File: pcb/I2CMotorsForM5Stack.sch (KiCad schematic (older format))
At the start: 14 parts, among them J1 free_holes, J2 Conn_01x04, J3 Conn_01x06, U1 TB6612FNG, U2 ATmega328P-AU

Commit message: Create pcb folder
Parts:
- U2: value ATmega328P-AU -> ATmega328P-MU; footprint Package_QFP:TQFP-32_7x7mm_P0.8mm -> Package_DFN_QFN:QFN-32-1EP_5x5mm_P0.5mm_EP3.1x3.1mm; symbol MCU_Microchip_ATmega:ATmega328P-AU -> MCU_Microchip_ATmega:ATmega328P-MU
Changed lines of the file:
@@
 $EndComp
 $Comp
-L MCU_Microchip_ATmega:ATmega328P-AU U2
+L MCU_Microchip_ATmega:ATmega328P-MU U2
 U 1 1 5E3FF990
 P 6750 3100
 F 0 "U2" H 6750 1511 50  0000 C CNN
-F 1 "ATmega328P-AU" H 6750 1420 50  0000 C CNN
-F 2 "Package_QFP:TQFP-32_7x7mm_P0.8mm" H 6750 3100 50  0001 C CIN
+F 1 "ATmega328P-MU" H 6750 1420 50  0000 C CNN
+F 2 "Package_DFN_QFN:QFN-32-1EP_5x5mm_P0.5mm_EP3.1x3.1mm" H 6750 3100 50  0001 C CIN
 F 3 "http://ww1.microchip.com/downloads/en/DeviceDoc/ATmega328_P%20AVR%20MCU%20with%20picoPower%20Technology%20Data%20Sheet%2040001984A.pdf" H 6750 3100 50  0001 C CNN
 	1    6750 3100

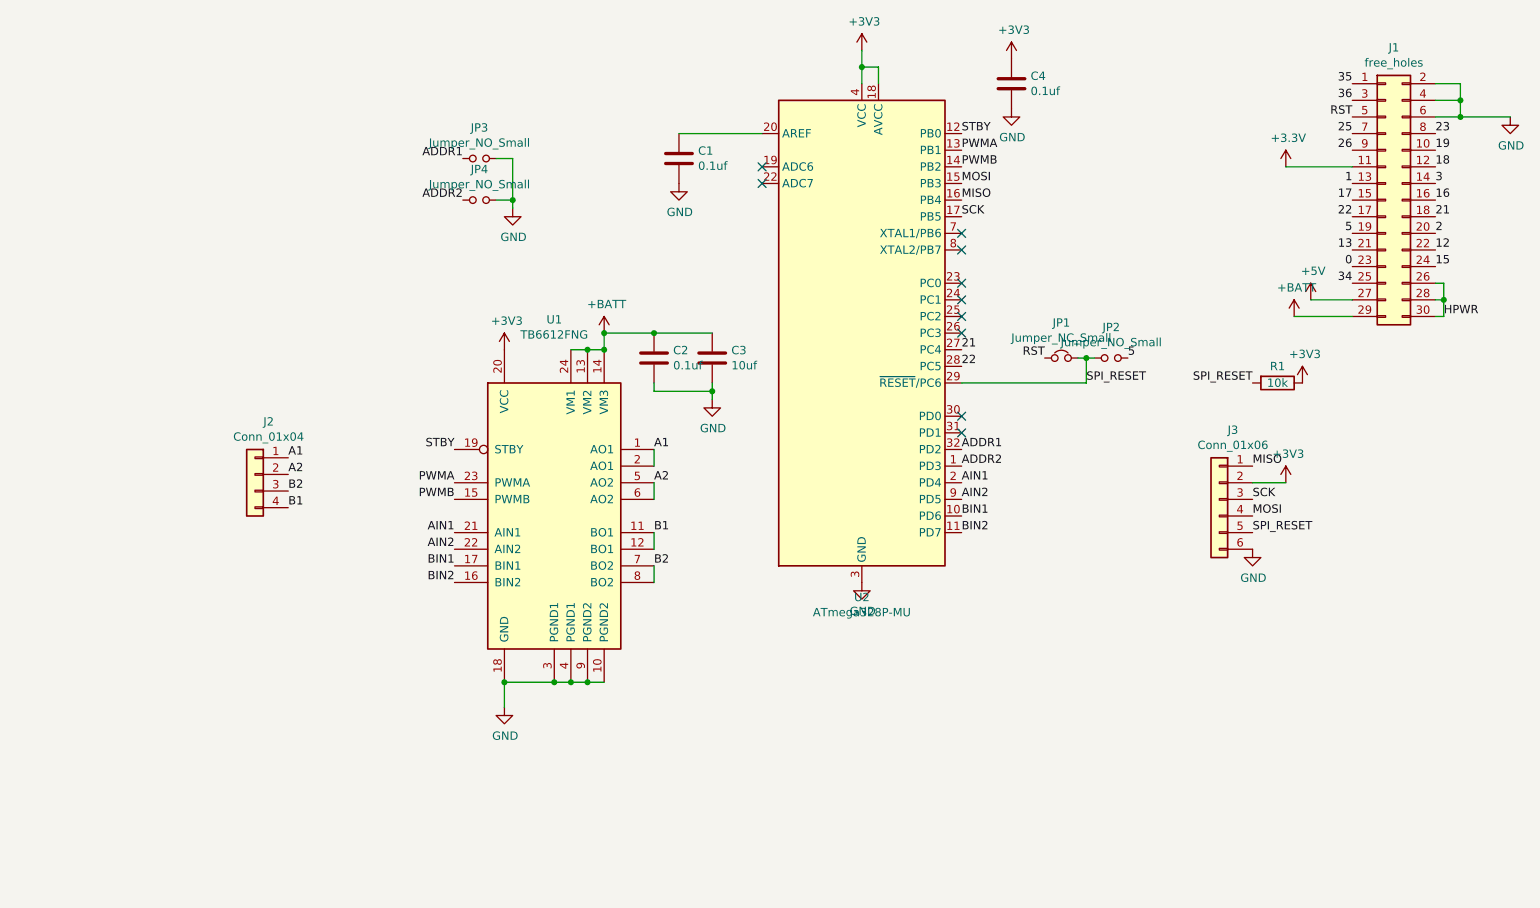
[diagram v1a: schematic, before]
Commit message: Put terminal mount out side of m5stack zone
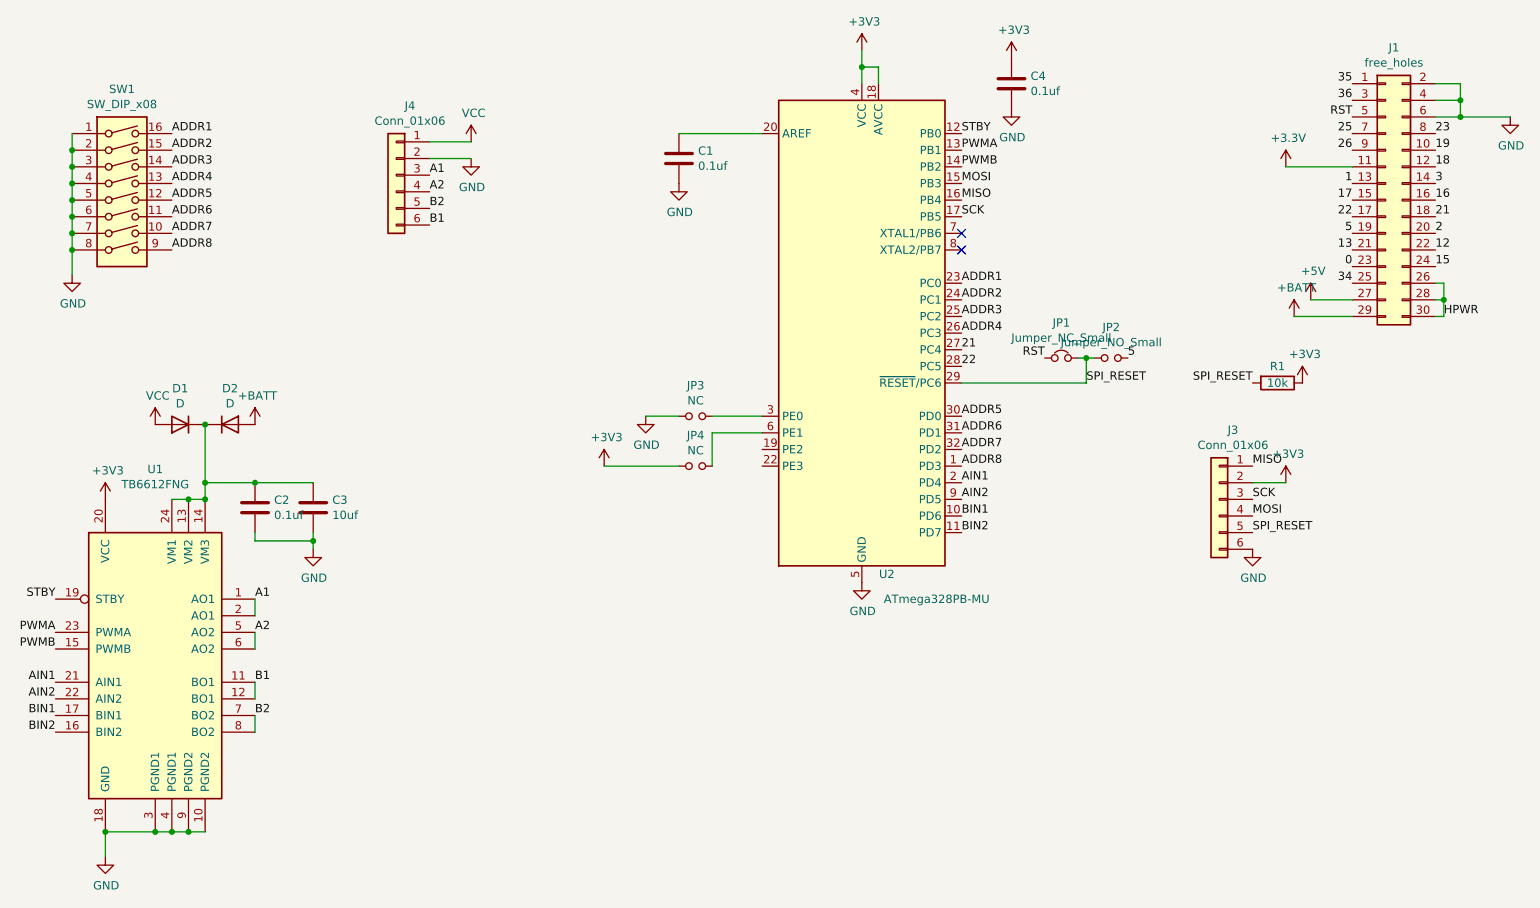
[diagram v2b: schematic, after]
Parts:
- removed J2: Conn_01x04, TerminalBlock:TerminalBlock_bornier-4_P5.08mm, symbol Connector_Generic:Conn_01x04
- removed U2: ATmega328P-MU, Package_DFN_QFN:QFN-32-1EP_5x5mm_P0.5mm_EP3.1x3.1mm, symbol MCU_Microchip_ATmega:ATmega328P-MU
- added D1, D2: D, Diode_SMD:D_SOD-123F, symbol Device:D
- added J4: Conn_01x06, TerminalBlock:TerminalBlock_bornier-6_P5.08mm, symbol Connector_Generic:Conn_01x06
- added SW1: SW_DIP_x08, Button_Switch_THT:SW_DIP_SPSTx08_Piano_CTS_Series194-8MSTN_W7.62mm_P2.54mm, symbol Switch:SW_DIP_x08
- added U2: ATmega328PB-MU, Package_DFN_QFN:QFN-32-1EP_5x5mm_P0.5mm_EP3.1x3.1mm, symbol MCU_Microchip_ATmega:ATmega328PB-MU
- J3: footprint Connector_PinHeader_2.54mm:PinHeader_2x03_P2.54mm_Vertical -> footprints:2x03_P2.54mm_Pads
- JP3, JP4: value Jumper_NO_Small -> NC
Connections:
- net +3V3: now also JP4.1, U2.18 (AVCC), U2.4 (VCC)
- net +BATT: now also D2.2 (A); no longer C2.1, C3.1, U1.13 (VM2), U1.14 (VM3), U1.24 (VM1)
- net 21: now also U2.27 (PC4)
- net 22: now also U2.28 (PC5)
- net A1: now also J4.3 (Pin_3)
- net A2: now also J4.4 (Pin_4)
- net ADDR1: now also SW1.16, U2.23 (PC0); no longer JP3.1
- net ADDR2: now also SW1.15, U2.24 (PC1); no longer JP4.1
- net AIN1: now also U2.2 (PD4)
- net AIN2: now also U2.9 (PD5)
- net B1: now also J4.6 (Pin_6)
- net B2: now also J4.5 (Pin_5)
- net BIN1: now also U2.10 (PD6)
- net BIN2: now also U2.11 (PD7)
- net GND: now also JP3.1, J4.2 (Pin_2), SW1.1, SW1.2, SW1.3, SW1.4, SW1.5, SW1.6, SW1.7, SW1.8, U2.21 (GND), U2.33 (GND), U2.5 (GND); no longer JP3.2, JP4.2
- net MISO: now also U2.16 (PB4)
- net MOSI: now also U2.15 (PB3)
- net PWMA: now also U2.13 (PB1)
- net PWMB: now also U2.14 (PB2)
- net SCK: now also U2.17 (PB5)
- net SPI_RESET: now also U2.29 (~RESET~/PC6)
- net STBY: now also U2.12 (PB0)
- net at C1.1: now also U2.20 (AREF)
- new net: C2.1, C3.1, D1.1 (K), D2.1 (K), U1.13 (VM2), U1.14 (VM3), U1.24 (VM1)
- new net: JP3.2, U2.3 (PE0)
- new net: JP4.2, U2.6 (PE1)
- new net ADDR3: SW1.14, U2.25 (PC2)
- new net ADDR4: SW1.13, U2.26 (PC3)
- new net ADDR5: SW1.12, U2.30 (PD0)
- new net ADDR6: SW1.11, U2.31 (PD1)
- new net ADDR7: SW1.10, U2.32 (PD2)
- new net ADDR8: SW1.9, U2.1 (PD3)
- new net VCC: D1.2 (A), J4.1 (Pin_1)
- no-connect marks 10 -> 2
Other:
- moved on the sheet: C2, C3, U1

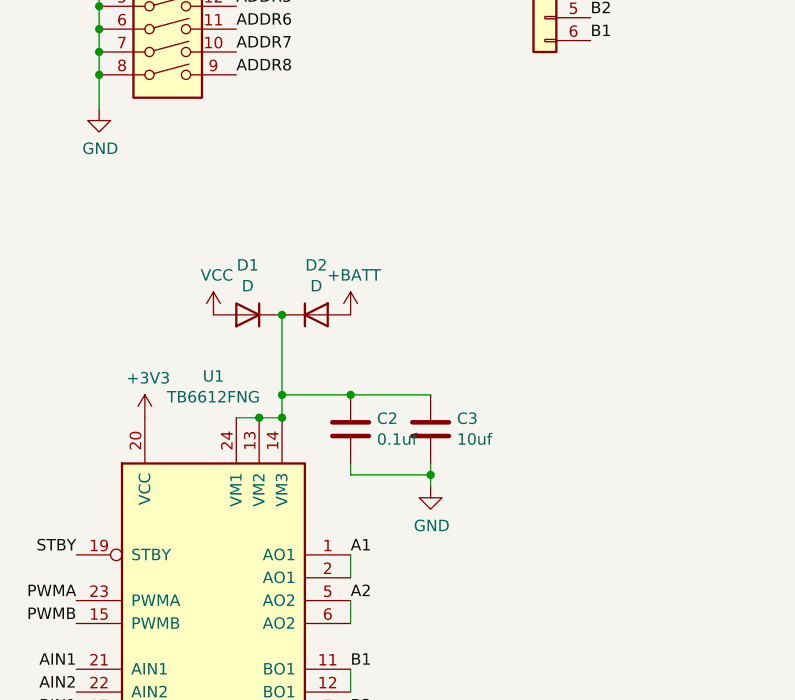
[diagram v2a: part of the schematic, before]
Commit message: Add diode to connect VM and GND
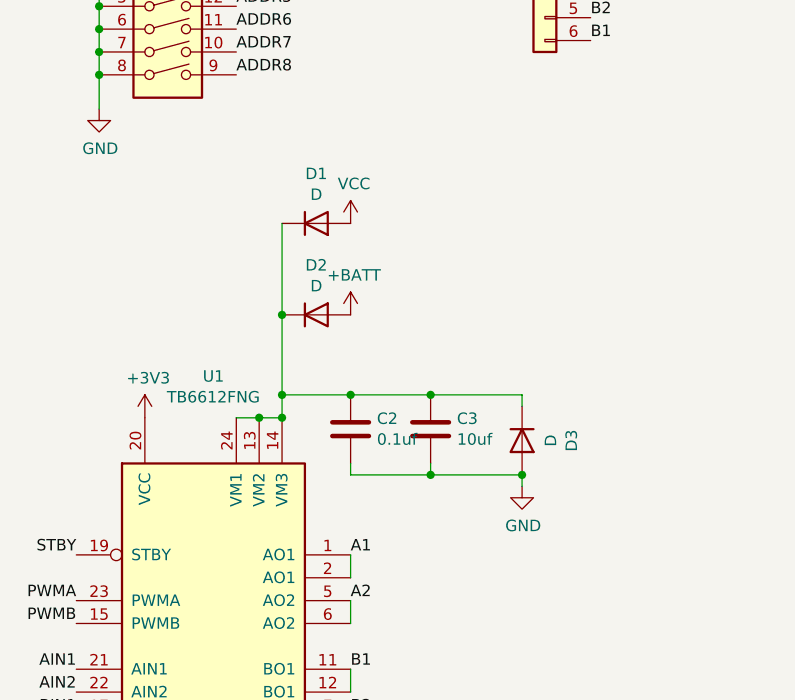
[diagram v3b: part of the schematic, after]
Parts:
- added D3: D, Diode_SMD:D_SOD-123F, symbol Device:D
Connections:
- net GND: now also D3.2 (A)
- net at C2.1, C3.1, D1.1 (K)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: now also D3.1 (K)
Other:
- moved on the sheet: D1
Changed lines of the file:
@@
 L power:GND #PWR0110
 U 1 1 5E435B2B
-P 3450 4400
-F 0 "#PWR0110" H 3450 4150 50  0001 C CNN
-F 1 "GND" H 3455 4227 50  0000 C CNN
-F 2 "" H 3450 4400 50  0001 C CNN
-F 3 "" H 3450 4400 50  0001 C CNN
-	1    3450 4400
-	1    0    0    -1
-$EndComp
-Wire Wire Line
-	3450 4400 3450 4350
+P 3850 4400
+F 0 "#PWR0110" H 3850 4150 50  0001 C CNN
+F 1 "GND" H 3855 4227 50  0000 C CNN
+F 2 "" H 3850 4400 50  0001 C CNN
+F 3 "" H 3850 4400 50  0001 C CNN
+	1    3850 4400
+	1    0    0    -1
+$EndComp
 Wire Wire Line
 	3450 4350 3100 4350
@@
 L Device:D D1
 U 1 1 5E687ABF
-P 2650 3650
-F 0 "D1" H 2650 3433 50  0000 C CNN
-F 1 "D" H 2650 3524 50  0000 C CNN
-F 2 "Diode_SMD:D_SOD-123F" H 2650 3650 50  0001 C CNN
-F 3 "~" H 2650 3650 50  0001 C CNN
-	1    2650 3650
-	-1   0    0    1
+P 2950 3250
+F 0 "D1" H 2950 3033 50  0000 C CNN
+F 1 "D" H 2950 3124 50  0000 C CNN
+F 2 "Diode_SMD:D_SOD-123F" H 2950 3250 50  0001 C CNN
+F 3 "~" H 2950 3250 50  0001 C CNN
+	1    2950 3250
+	1    0    0    1
 $EndComp
 Wire Wire Line
@@
 L power:VCC #PWR0118
 U 1 1 5E689725
-P 2500 3650
-F 0 "#PWR0118" H 2500 3500 50  0001 C CNN
-F 1 "VCC" H 2515 3823 50  0000 C CNN
-F 2 "" H 2500 3650 50  0001 C CNN
-F 3 "" H 2500 3650 50  0001 C CNN
-	1    2500 3650
+P 3100 3250
+F 0 "#PWR0118" H 3100 3100 50  0001 C CNN
+F 1 "VCC" H 3115 3423 50  0000 C CNN
+F 2 "" H 3100 3250 50  0001 C CNN
+F 3 "" H 3100 3250 50  0001 C CNN
+	1    3100 3250
 	1    0    0    -1
 $EndComp
@@
 Wire Wire Line
 	5200 3900 5650 3900
+Wire Wire Line
+	2800 3250 2800 3650
+$Comp
+L Device:D D3
+U 1 1 5E82611F
+P 3850 4200
+F 0 "D3" H 3850 4417 50  0000 C CNN
+F 1 "D" H 3850 4326 50  0000 C CNN
+F 2 "Diode_SMD:D_SOD-123F" H 3850 4200 50  0001 C CNN
+F 3 "~" H 3850 4200 50  0001 C CNN
+	1    3850 4200
+	0    1    1    0
+$EndComp
+Wire Wire Line
+	3850 4050 3850 4000
+Wire Wire Line
+	3850 4000 3450 4000
+Connection ~ 3450 4000
+Wire Wire Line
+	3850 4400 3850 4350
+Wire Wire Line
+	3850 4350 3450 4350
+Connection ~ 3850 4350
 $EndSCHEMATC

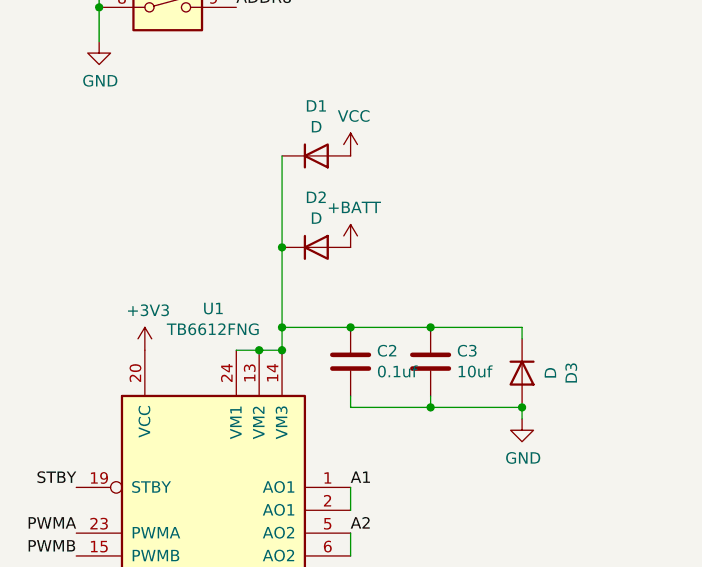
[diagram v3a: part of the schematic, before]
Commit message: Assign thick line to motor power
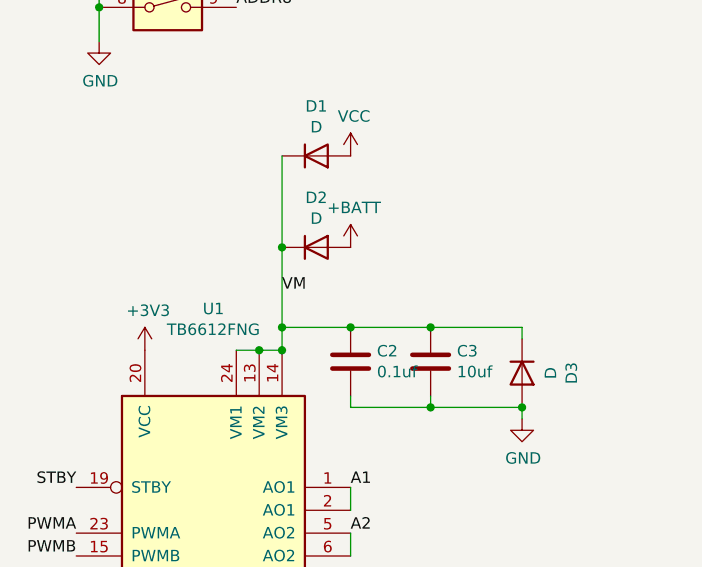
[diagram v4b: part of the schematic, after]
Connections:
- net VM: now reaches C2.1, C3.1, D1.1 (K), D2.1 (K), D3.1 (K), U1.13 (VM2), U1.14 (VM3), U1.24 (VM1)
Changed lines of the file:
@@
 	3850 4350 3450 4350
 Connection ~ 3850 4350
+Text Label 2800 3850 0    50   ~ 0
+VM
 $EndSCHEMATC
